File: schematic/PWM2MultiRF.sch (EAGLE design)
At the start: 20 parts, among them J1 MICRO_USB_B_MALE_HIROSE_ZX80-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, Q4 8MHz, U1 ATMEGA328L, U2 ###V, U3 HC_05

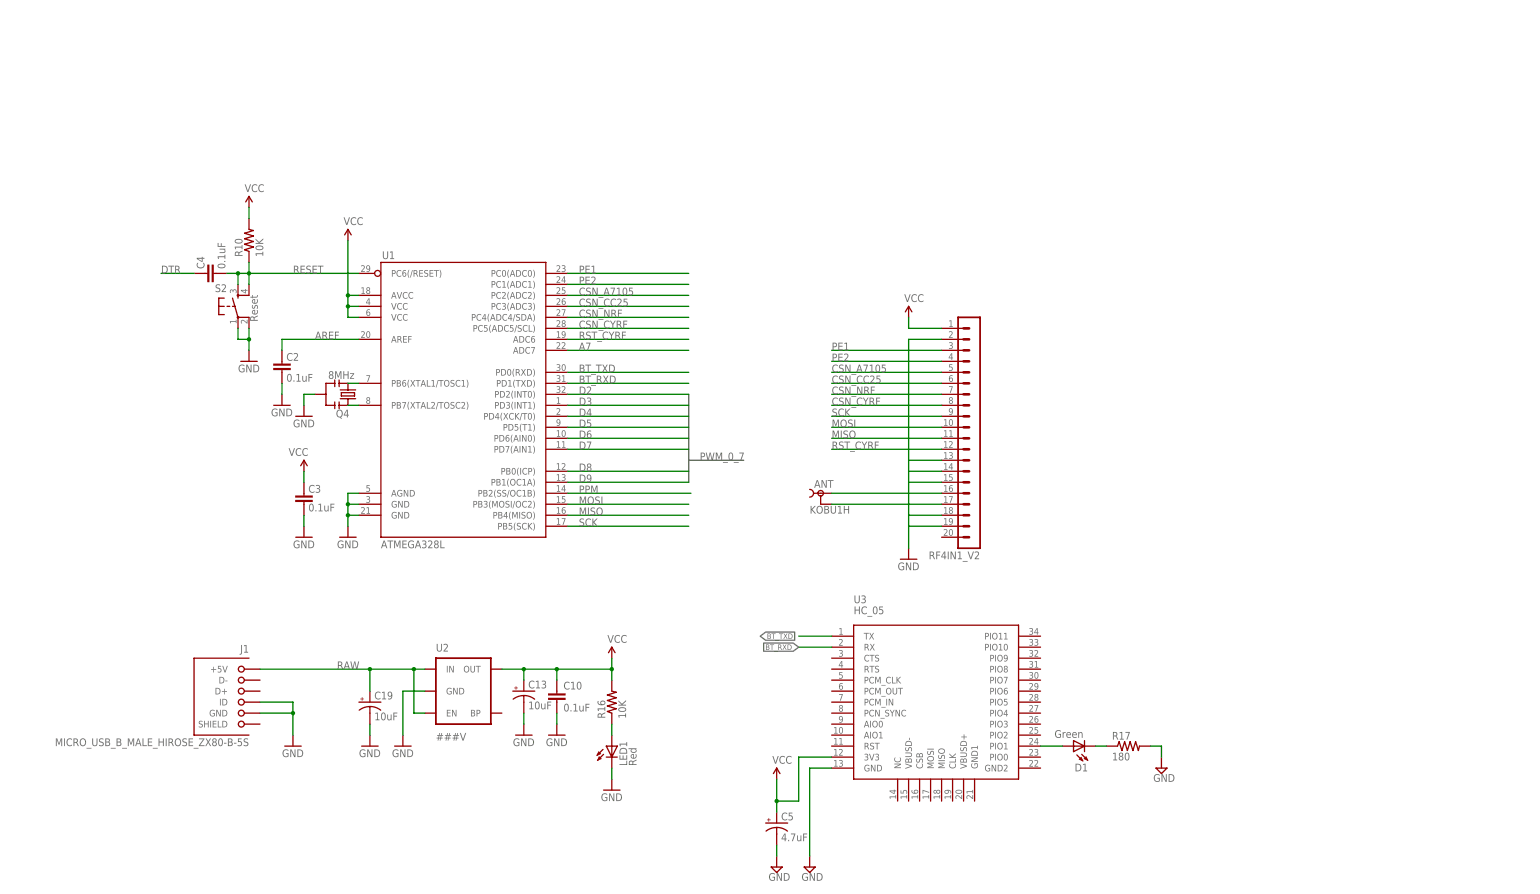
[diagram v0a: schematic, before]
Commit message: 9XR module added
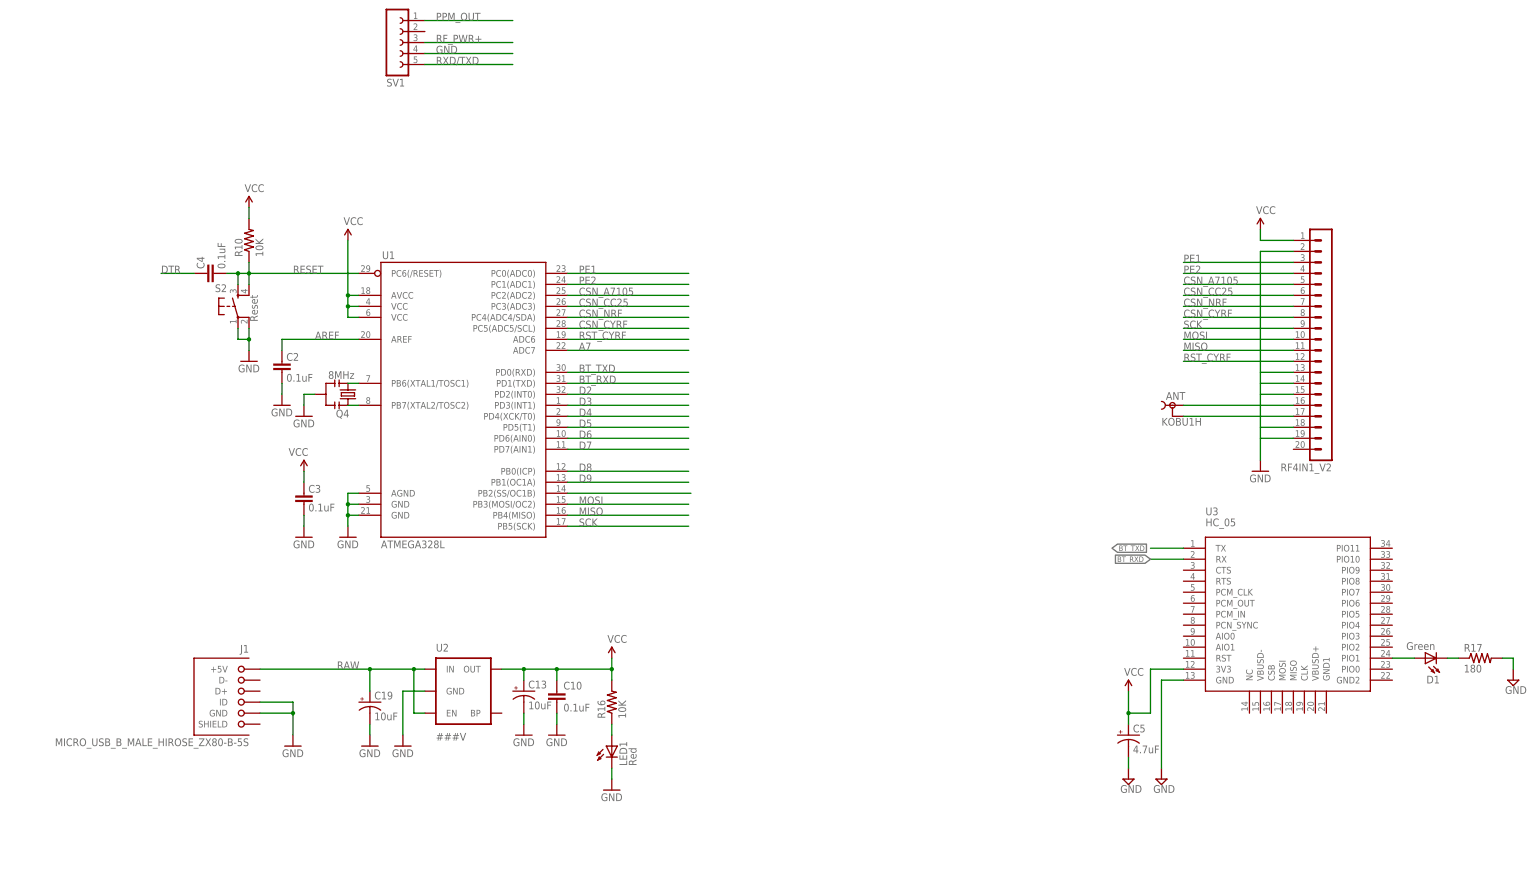
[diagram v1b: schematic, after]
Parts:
- added SV1: (no value), con-lsta:FE05W
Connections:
- new net PPM_OUT: SV1.1
- new net RF_PWR+: SV1.3
- new net RXD/TXD: SV1.5
- net GND: now also SV1.4
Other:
- moved on the sheet: ANT, C5, D1, R17, RF4IN1_V2, U3
